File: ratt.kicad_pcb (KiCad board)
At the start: 2 copper layers, 40.6 x 30.7 mm, 35 parts, among them J1 Conn_01x04_Male, J2 Conn_01x04_Male, Q1 2N5457, U1 LM308N

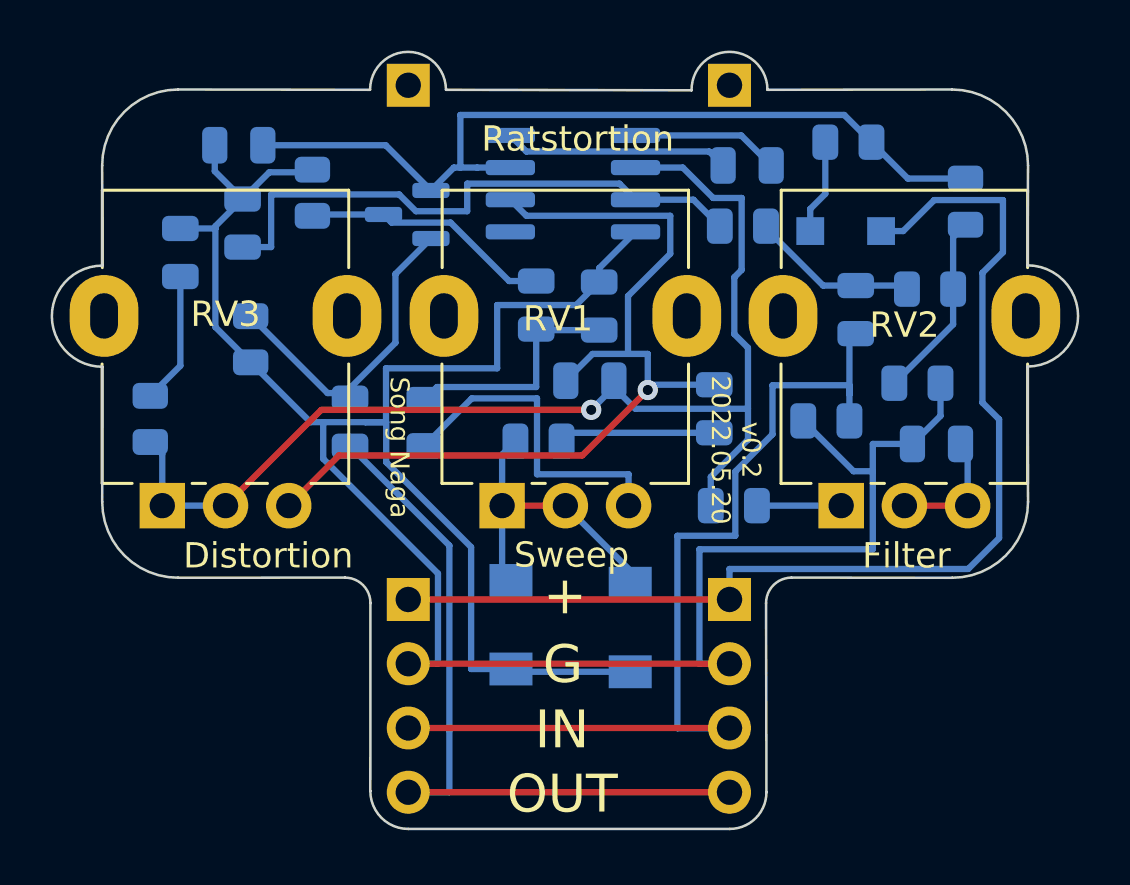
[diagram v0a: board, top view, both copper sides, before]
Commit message: updated rotation of pots.
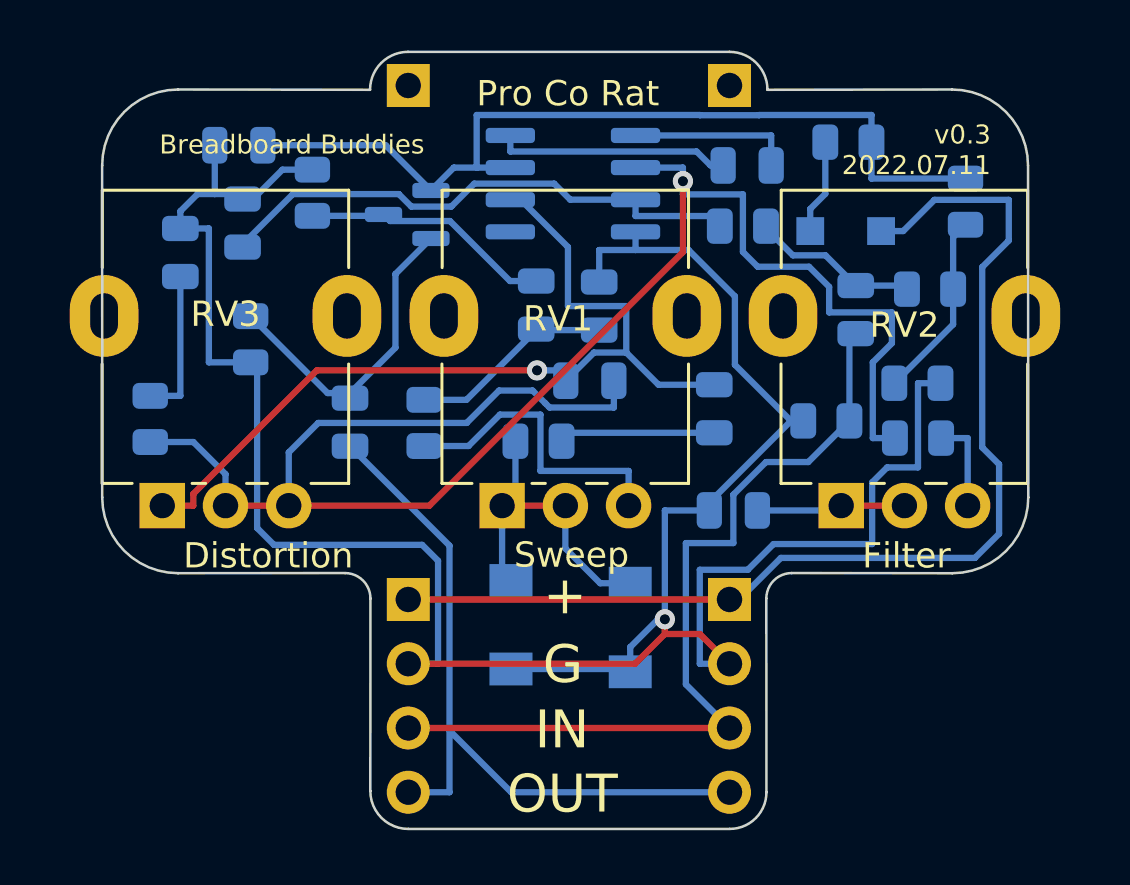
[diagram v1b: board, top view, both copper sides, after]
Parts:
- removed REF1, REF2: PinHeader_1x01_P2.54mm_Vertical, Connector_PinHeader_2.54mm:PinHeader_1x01_P2.54mm_Vertical
- added G1: LOGO, LOGO, B.Cu at (35.8, 51.8)
- added J3: Conn_01x01_Male, Connector_PinSocket_2.54mm:PinSocket_1x01_P2.54mm_Vertical, B.Cu at (29.4, 24.2)
- added J4: Conn_01x01_Male, Connector_PinSocket_2.54mm:PinSocket_1x01_P2.54mm_Vertical, B.Cu at (42.1, 24.2)
- moved C10 8.45 mm to (42.3, 41.0)
- moved R8 7.75 mm to (49.6, 38.2)
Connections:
- RV2 pad 1: Net-(R8-Pad1) -> Net-(C10-Pad1)
- RV2 pad 3: Net-(C10-Pad1) -> Net-(R8-Pad1)
- RV3 pad 1: Net-(C8-Pad1) -> Net-(C2-Pad1)
- RV3 pad 3: Net-(C2-Pad1) -> Net-(C8-Pad1)
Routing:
- net Net-(C8-Pad1): track 46.2 -> 68.3 mm
- net INPUT: track 38.2 -> 33.9 mm
- net Net-(C2-Pad1): track 36.6 -> 35.0 mm
- net Net-(C4-Pad1): track 23.0 -> 21.5 mm
- net Net-(C3-Pad1): track 9.42 -> 8.10 mm
- net GND: track 105.4 -> 104.4 mm, vias 0 -> 1
- net Net-(R4-Pad1): track 13.1 -> 12.2 mm
- net Net-(C10-Pad1): track 5.06 -> 5.89 mm
- net VA: track 34.0 -> 34.8 mm
- net Net-(C11-Pad1): track 5.21 -> 5.91 mm
- net Net-(D1-Pad2): track 12.5 -> 13.2 mm
- net Net-(C6-Pad2): track 5.85 -> 6.55 mm
- net OUTPUT: track 29.6 -> 29.0 mm
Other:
- board size 40.6 x 30.7 mm -> 36.6 x 30.7 mm
- board text added: "Breadboard Buddies"
- board text added: "Pro Co Rat"
- board text added: "v0.3 2022.07.11"
- board text removed: "Ratstortion"
- board text removed: "Song Naga"
- board text removed: "v0.2 2022.05.20"
